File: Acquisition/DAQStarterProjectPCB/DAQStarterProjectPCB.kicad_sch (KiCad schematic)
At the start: 2 parts, among them U1 LSM6DS3TR, U2 STM32F042K6T6

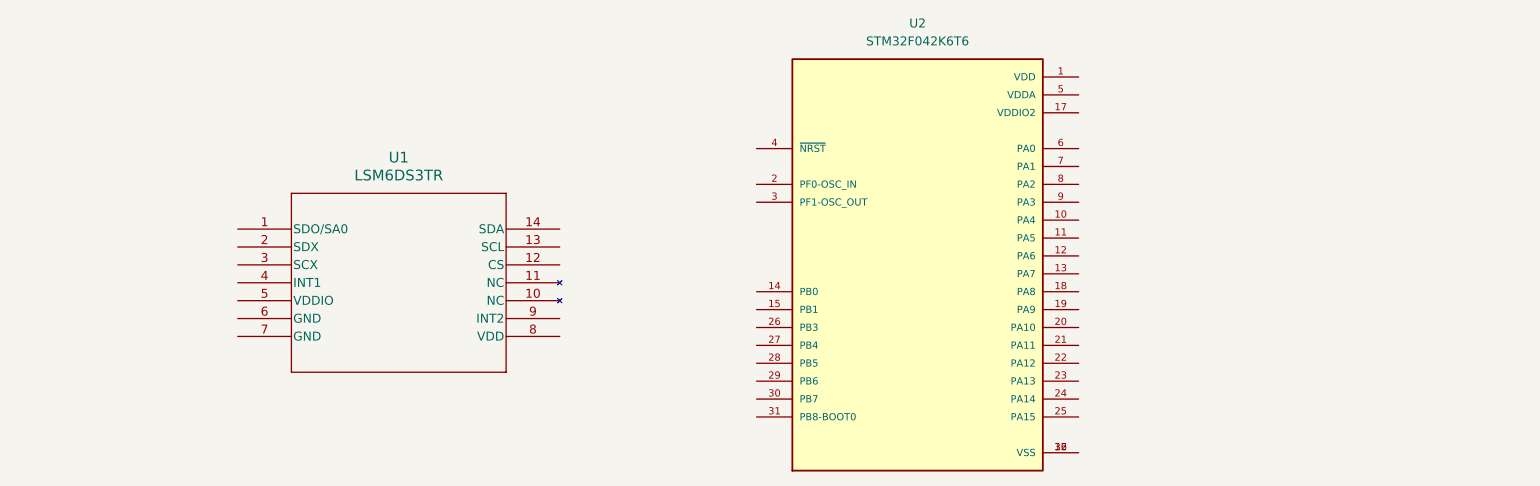
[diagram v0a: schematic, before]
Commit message: added usb sym
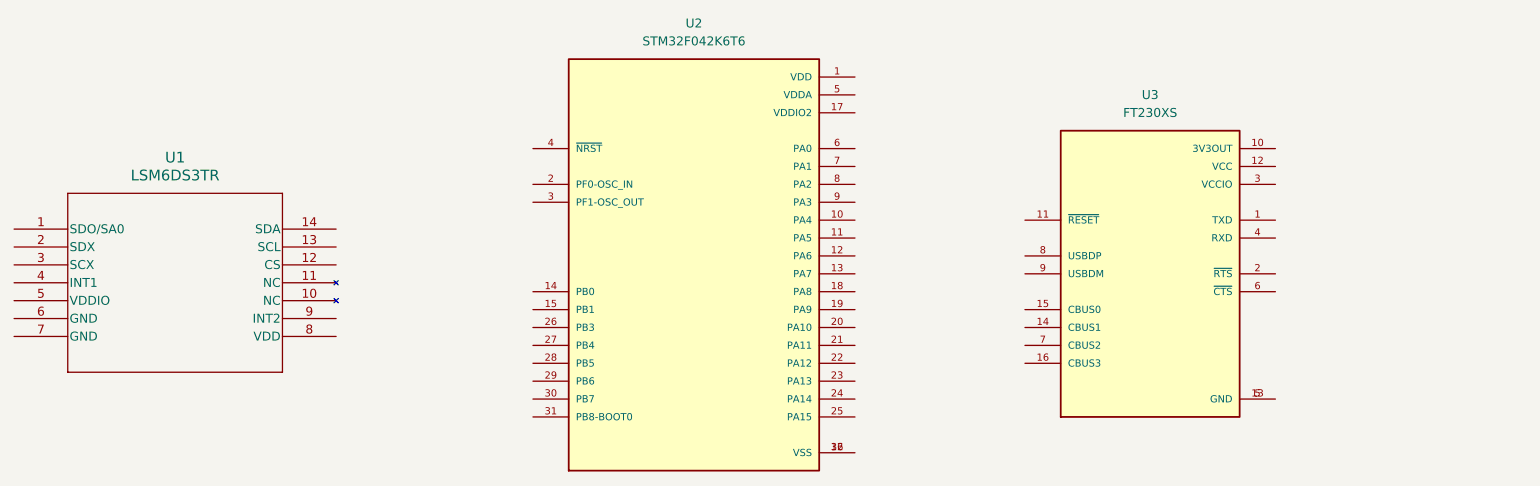
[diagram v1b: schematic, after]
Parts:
- added U3: FT230XS, USBSym:SOP63P599X175-16N, symbol FT230XS:FT230XS
- U1: footprint LGA-14L_2P5X3X0P83_STM -> footprints:LGA-14L_2P5X3X0P83_STM
- U2: footprint STM32F042K6T6:QFP80P900X900X160-32N -> MCUSym:QFP80P900X900X160-32N
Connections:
- new net: U3.13 (GND), U3.5 (GND)
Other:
- moved on the sheet: U1, U2

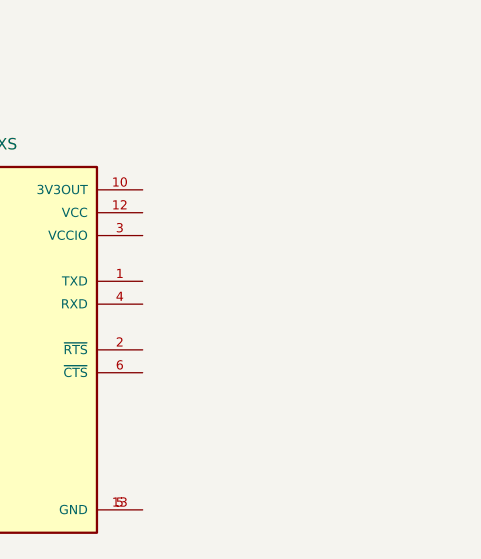
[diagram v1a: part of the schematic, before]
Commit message: Added USB_A Connector
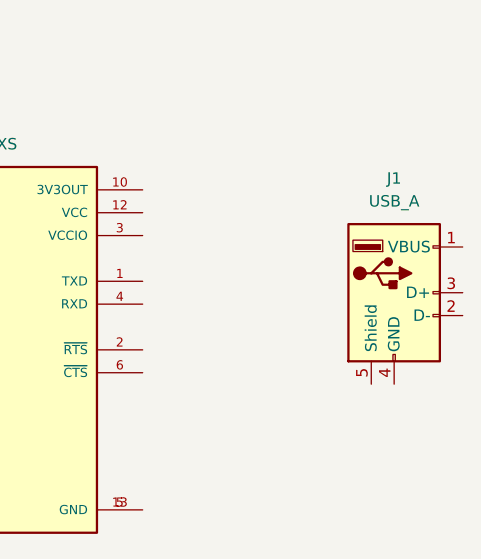
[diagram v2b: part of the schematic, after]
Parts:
- added J1: USB_A, symbol Connector:USB_A
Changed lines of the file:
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@@
 		)
 		(instances
-			(project ""
+			(project "DAQStarterProjectPCB"
 				(path "/9c8ab052-4b6c-4266-9718-063ad4ad6811"
 					(reference "U2")
+					(unit 1)
+				)
+			)
+		)
+	)
+	(symbol
+		(lib_id "Connector:USB_A")
+		(at 264.16 91.44 0)
+		(unit 1)
+		(exclude_from_sim no)
+		(in_bom yes)
+		(on_board yes)
+		(dnp no)
+		(fields_autoplaced yes)
+		(property "Reference" "J1"
+			(at 264.16 78.74 0)
+			(effects
+				(font
+					(size 1.27 1.27)
+				)
+			)
+		)
+		(property "Value" "USB_A"
+			(at 264.16 81.28 0)
+			(effects
+				(font
+					(size 1.27 1.27)
+				)
+			)
+		)
+		(property "Footprint" ""
+			(at 267.97 92.71 0)
+			(effects
+				(font
+					(size 1.27 1.27)
+				)
+				(hide yes)
+			)
+		)
+		(property "Datasheet" " ~"
+			(at 267.97 92.71 0)
+			(effects
+				(font
+					(size 1.27 1.27)
+				)
+				(hide yes)
+			)
+		)
+		(property "Description" "USB Type A connector"
+			(at 264.16 91.44 0)
+			(effects
+				(font
+					(size 1.27 1.27)
+				)
+				(hide yes)
+			)
+		)
+		(pin "3"
+		)
+		(pin "4"
+		)
+		(pin "5"
+		)
+		(pin "2"
+		)
+		(pin "1"
+		)
+		(instances
+			(project "DAQStarterProjectPCB"
+				(path "/9c8ab052-4b6c-4266-9718-063ad4ad6811"
+					(reference "J1")
 					(unit 1)
 				)
@@
 		)
 		(instances
-			(project ""
+			(project "DAQStarterProjectPCB"
 				(path "/9c8ab052-4b6c-4266-9718-063ad4ad6811"
 					(reference "U1")
@@
 		)
 		(instances
-			(project ""
+			(project "DAQStarterProjectPCB"
 				(path "/9c8ab052-4b6c-4266-9718-063ad4ad6811"
 					(reference "U3")
